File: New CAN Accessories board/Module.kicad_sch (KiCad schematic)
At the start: 13 parts, among them J1 39301040, Q1 IRLML6344TRPBF

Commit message: post design review
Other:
- moved on the sheet: TPgt1
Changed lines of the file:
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@@
+	)
+	(junction
+		(at 67.31 24.13)
+		(diameter 0)
+		(color 0 0 0 0)
 	)
 	(junction
@@
 	(wire
 		(pts
+			(xy 33.02 78.74) (xy 33.02 83.82)
+		)
+		(stroke
+			(width 0)
+			(type default)
+		)
+	)
+	(wire
+		(pts
 			(xy 40.64 63.5) (xy 43.18 63.5)
 		)
@@
 	(wire
 		(pts
+			(xy 69.85 24.13) (xy 67.31 24.13)
+		)
+		(stroke
+			(width 0)
+			(type default)
+		)
+	)
+	(wire
+		(pts
 			(xy 38.1 76.2) (xy 40.64 76.2)
+		)
+		(stroke
+			(width 0)
+			(type default)
+		)
+	)
+	(wire
+		(pts
+			(xy 15.24 78.74) (xy 33.02 78.74)
 		)
 		(stroke
@@
 	(hierarchical_label "OA"
 		(shape input)
-		(at 67.31 24.13 0)
+		(at 69.85 24.13 0)
 		(effects
 			(font
@@
 	(symbol
 		(lib_id "Connector:TestPoint")
-		(at 33.02 83.82 0)
+		(at 15.24 78.74 0)
 		(unit 1)
 		(exclude_from_sim no)
@@
 		(fields_autoplaced yes)
 		(property "Reference" "TPgt1"
-			(at 35.56 79.2479 0)
+			(at 17.78 74.1679 0)
 			(effects
 				(font
@@
 		)
 		(property "Value" "TestPoint"
-			(at 35.56 81.7879 0)
+			(at 17.78 76.7079 0)
 			(effects
 				(font
@@
 		)
 		(property "Footprint" "Connector_PinHeader_1.00mm:PinHeader_1x01_P1.00mm_Vertical"
-			(at 38.1 83.82 0)
+			(at 20.32 78.74 0)
 			(effects
 				(font
@@
 		)
 		(property "Datasheet" "~"
-			(at 38.1 83.82 0)
+			(at 20.32 78.74 0)
 			(effects
 				(font
@@
 		)
 		(property "Description" "test point"
-			(at 33.02 83.82 0)
-			(effects
-				(font
+			(at 15.24 78.74 0)
+			(effects
+				(font

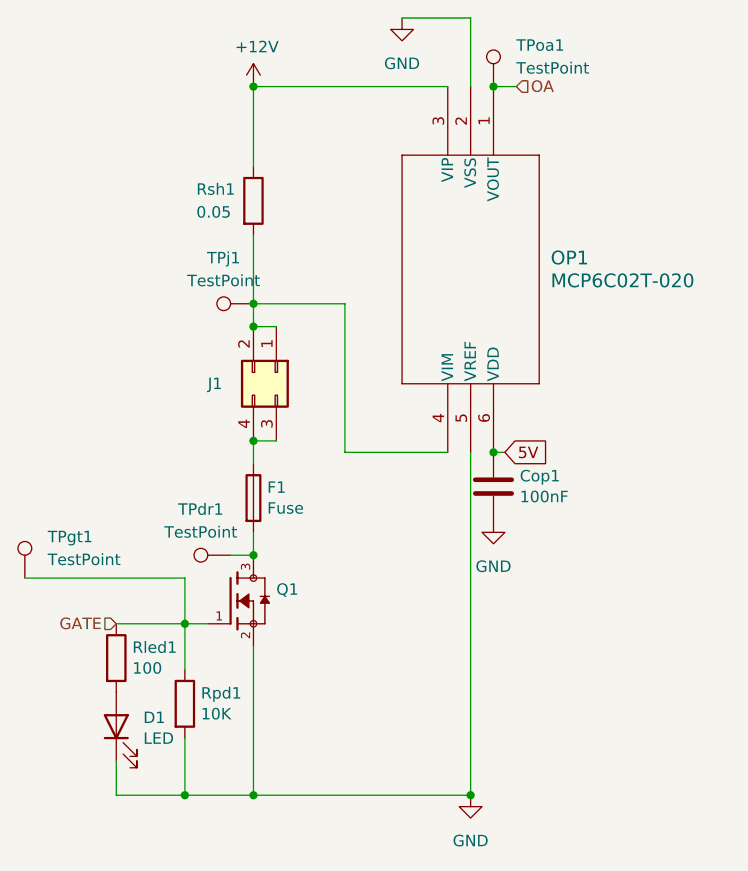
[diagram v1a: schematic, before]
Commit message: Added test points 1x12 pin and 1x8 pin
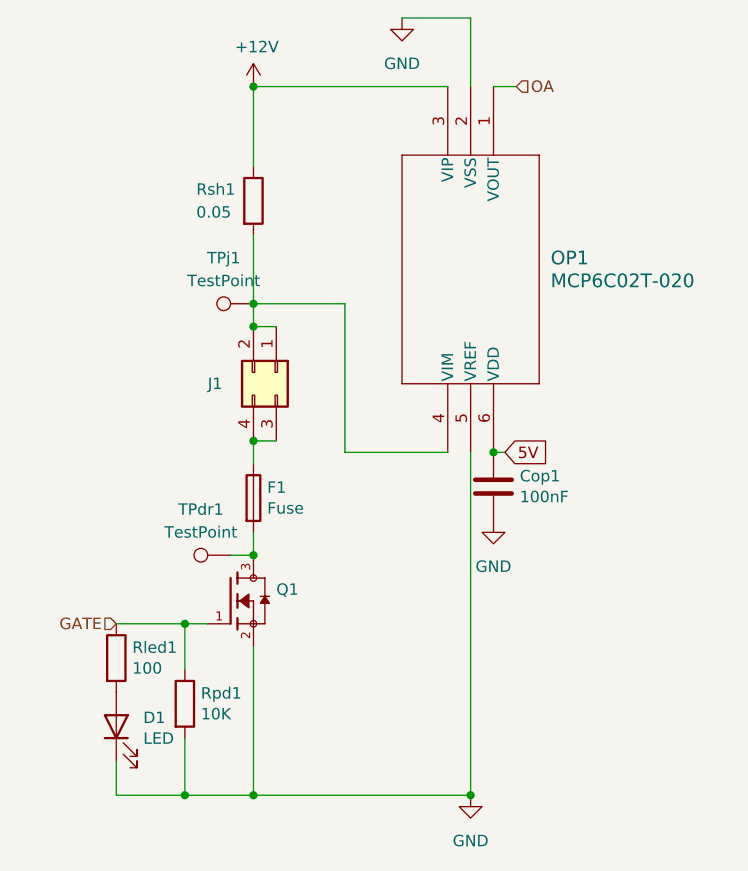
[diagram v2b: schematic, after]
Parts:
- removed TPgt1, TPoa1: TestPoint, Connector_PinHeader_1.00mm:PinHeader_1x01_P1.00mm_Vertical, symbol Connector:TestPoint
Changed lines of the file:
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@@
-	)
-	(junction
-		(at 67.31 24.13)
-		(diameter 0)
-		(color 0 0 0 0)
 	)
 	(junction
@@
 	(wire
 		(pts
-			(xy 33.02 78.74) (xy 33.02 83.82)
-		)
-		(stroke
-			(width 0)
-			(type default)
-		)
-	)
-	(wire
-		(pts
 			(xy 40.64 63.5) (xy 43.18 63.5)
 		)
@@
 		(pts
 			(xy 38.1 76.2) (xy 40.64 76.2)
-		)
-		(stroke
-			(width 0)
-			(type default)
-		)
-	)
-	(wire
-		(pts
-			(xy 15.24 78.74) (xy 33.02 78.74)
 		)
 		(stroke
@@
 	)
 	(symbol
-		(lib_id "Connector:TestPoint")
-		(at 67.31 24.13 0)
-		(unit 1)
-		(exclude_from_sim no)
-		(in_bom yes)
-		(on_board yes)
-		(dnp no)
-		(fields_autoplaced yes)
-		(property "Reference" "TPoa1"
-			(at 69.85 19.5579 0)
-			(effects
-				(font
-					(size 1.27 1.27)
-				)
-				(justify left)
-			)
-		)
-		(property "Value" "TestPoint"
-			(at 69.85 22.0979 0)
-			(effects
-				(font
-					(size 1.27 1.27)
-				)
-				(justify left)
-			)
-		)
-		(property "Footprint" "Connector_PinHeader_1.00mm:PinHeader_1x01_P1.00mm_Vertical"
-			(at 72.39 24.13 0)
-			(effects
-				(font
-					(size 1.27 1.27)
-				)
-				(hide yes)
-			)
-		)
-		(property "Datasheet" "~"
-			(at 72.39 24.13 0)
-			(effects
-				(font
-					(size 1.27 1.27)
-				)
-				(hide yes)
-			)
-		)
-		(property "Description" "test point"
-			(at 67.31 24.13 0)
-			(effects
-				(font
-					(size 1.27 1.27)
-				)
-				(hide yes)
-			)
-		)
-		(pin "1"
-		)
-		(instances
-			(project "New CAN Accessories board"
-				(path "/88340f43-3f46-45a6-9393-130e00dc3071/066a2d54-ef62-4b50-bc17-9ae15f85282f"
-					(reference "TPoa3")
-					(unit 1)
-				)
-				(path "/88340f43-3f46-45a6-9393-130e00dc3071/199d9661-d77c-40a8-9127-2f77ddd20cbc"
-					(reference "TPoa2")
-					(unit 1)
-				)
-				(path "/88340f43-3f46-45a6-9393-130e00dc3071/a4a3a29c-d4d7-4a64-89ca-c4c515902e3a"
-					(reference "TPoa8")
-					(unit 1)
-				)
-				(path "/88340f43-3f46-45a6-9393-130e00dc3071/b4fef664-0317-4528-b914-9a729a4fa0cb"
-					(reference "TPoa7")
-					(unit 1)
-				)
-				(path "/88340f43-3f46-45a6-9393-130e00dc3071/df424b4d-8c7c-4d94-be97-d7e7a5882dfa"
-					(reference "TPoa6")
-					(unit 1)
-				)
-				(path "/88340f43-3f46-45a6-9393-130e00dc3071/e28dd46e-a6b0-42fd-b358-90f6a987ac56"
-					(reference "TPoa4")
-					(unit 1)
-				)
-				(path "/88340f43-3f46-45a6-9393-130e00dc3071/f4946d2d-97a8-44f8-9d9c-ff737967b4cd"
-					(reference "TPoa5")
-					(unit 1)
-				)
-				(path "/88340f43-3f46-45a6-9393-130e00dc3071/fb19124a-c234-4595-adc5-bbb1e37c8292"
-					(reference "TPoa1")
-					(unit 1)
-				)
-			)
-		)
-	)
-	(symbol
 		(lib_id "Device:Fuse")
 		(at 40.64 69.85 0)
@@
 					(unit 1)
 				)
-			)
-		)
-	)
-	(symbol
-		(lib_id "Connector:TestPoint")
-		(at 15.24 78.74 0)
-		(unit 1)
-		(exclude_from_sim no)
-		(in_bom yes)
-		(on_board yes)
-		(dnp no)
-		(fields_autoplaced yes)
-		(property "Reference" "TPgt1"
-			(at 17.78 74.1679 0)
-			(effects
-				(font
-					(size 1.27 1.27)
-				)
-				(justify left)
-			)
-		)
-		(property "Value" "TestPoint"
-			(at 17.78 76.7079 0)
-			(effects
-				(font
-					(size 1.27 1.27)
-				)
-				(justify left)
-			)
-		)
-		(property "Footprint" "Connector_PinHeader_1.00mm:PinHeader_1x01_P1.00mm_Vertical"
-			(at 20.32 78.74 0)
-			(effects
-				(font
-					(size 1.27 1.27)
-				)
-				(hide yes)
-			)
-		)
-		(property "Datasheet" "~"
-			(at 20.32 78.74 0)
-			(effects
-				(font
-					(size 1.27 1.27)
-				)
-				(hide yes)
-			)
-		)
-		(property "Description" "test point"
-			(at 15.24 78.74 0)
-			(effects
-				(font
-					(size 1.27 1.27)
-				)
-				(hide yes)
-			)
-		)
-		(pin "1"
-		)
-		(instances
-			(project "New CAN Accessories board"
-				(path "/88340f43-3f46-45a6-9393-130e00dc3071/066a2d54-ef62-4b50-bc17-9ae15f85282f"
-					(reference "TPgt3")
-					(unit 1)
-				)
-				(path "/88340f43-3f46-45a6-9393-130e00dc3071/199d9661-d77c-40a8-9127-2f77ddd20cbc"
-					(reference "TPgt2")
-					(unit 1)
-				)
-				(path "/88340f43-3f46-45a6-9393-130e00dc3071/a4a3a29c-d4d7-4a64-89ca-c4c515902e3a"
-					(reference "TPgt8")
-					(unit 1)
-				)
-				(path "/88340f43-3f46-45a6-9393-130e00dc3071/b4fef664-0317-4528-b914-9a729a4fa0cb"
-					(reference "TPgt7")
-					(unit 1)
-				)
-				(path "/88340f43-3f46-45a6-9393-130e00dc3071/df424b4d-8c7c-4d94-be97-d7e7a5882dfa"
-					(reference "TPgt6")
-					(unit 1)
-				)
-				(path "/88340f43-3f46-45a6-9393-130e00dc3071/e28dd46e-a6b0-42fd-b358-90f6a987ac56"
-					(reference "TPgt4")
-					(unit 1)
-				)
-				(path "/88340f43-3f46-45a6-9393-130e00dc3071/f4946d2d-97a8-44f8-9d9c-ff737967b4cd"
-					(reference "TPgt5")
-					(unit 1)
-				)
-				(path "/88340f43-3f46-45a6-9393-130e00dc3071/fb19124a-c234-4595-adc5-bbb1e37c8292"
-					(reference "TPgt1")
-					(unit 1)
-				)

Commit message: Added two 1x4 pin headers for J1-J8 - also fixed CAN module
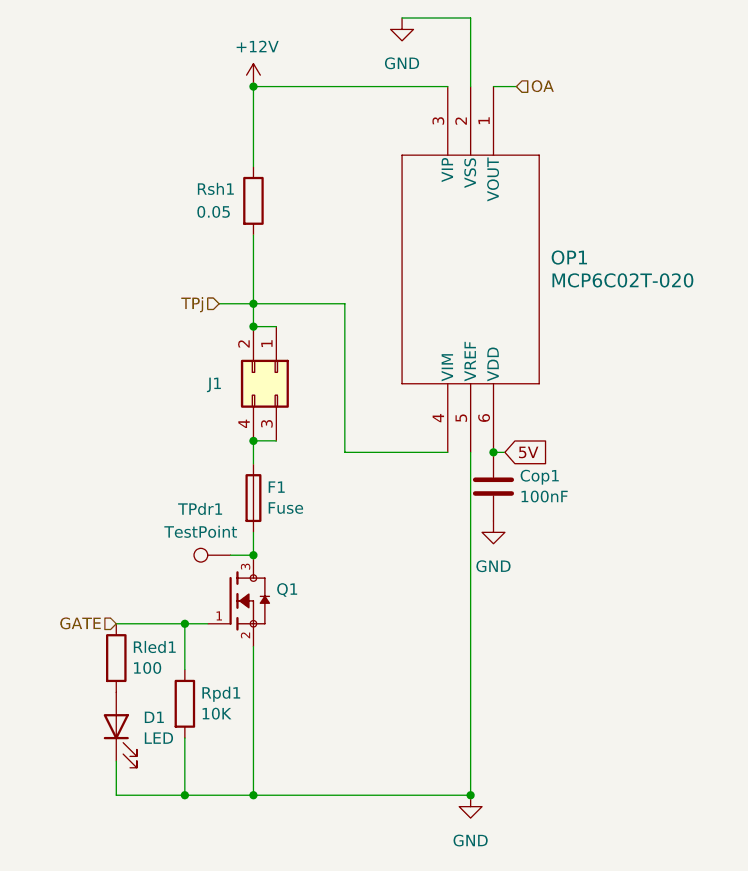
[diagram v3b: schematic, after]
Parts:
- removed TPj1: TestPoint, Connector_PinHeader_1.00mm:PinHeader_1x01_P1.00mm_Vertical, symbol Connector:TestPoint
- TPdr1: footprint Connector_PinHeader_1.00mm:PinHeader_1x01_P1.00mm_Vertical -> Connector_PinHeader_2.54mm:PinHeader_1x01_P2.54mm_Vertical
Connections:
- net TPj: now reaches J1.1 (Pin_1), J1.2 (Pin_2), OP1.4 (VIM), Rsh1.2
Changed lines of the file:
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@@
+	(wire
+		(pts
+			(xy 36.83 48.26) (xy 40.64 48.26)
+		)
+		(stroke
+			(width 0)
+			(type default)
+		)
+	)
 	(wire
 		(pts
@@
 				(hide yes)
 			)
+		)
+	)
+	(hierarchical_label "TPj"
+		(shape input)
+		(at 36.83 48.26 180)
+		(effects
+			(font
+				(size 1.27 1.27)
+			)
+			(justify right)
 		)
 	)
@@
 			)
 		)
-		(property "Footprint" "Connector_PinHeader_1.00mm:PinHeader_1x01_P1.00mm_Vertical"
+		(property "Footprint" "Connector_PinHeader_2.54mm:PinHeader_1x01_P2.54mm_Vertical"
 			(at 38.1 71.12 0)
 			(effects
@@
 				)
 				(hide yes)
+			)
+		)
+		(property "Purpose" ""
+			(at 38.1 76.2 0)
+			(effects
+				(font
+					(size 1.27 1.27)
+				)
 			)
 		)
@@
 					(unit 1)
 				)
-			)
-		)
-	)
-	(symbol
-		(lib_id "Connector:TestPoint")
-		(at 40.64 48.26 90)
-		(unit 1)
-		(exclude_from_sim no)
-		(in_bom yes)
-		(on_board yes)
-		(dnp no)
-		(fields_autoplaced yes)
-		(property "Reference" "TPj1"
-			(at 37.338 43.18 90)
-			(effects
-				(font
-					(size 1.27 1.27)
-				)
-			)
-		)
-		(property "Value" "TestPoint"
-			(at 37.338 45.72 90)
-			(effects
-				(font
-					(size 1.27 1.27)
-				)
-			)
-		)
-		(property "Footprint" "Connector_PinHeader_1.00mm:PinHeader_1x01_P1.00mm_Vertical"
-			(at 40.64 43.18 0)
-			(effects
-				(font
-					(size 1.27 1.27)
-				)
-				(hide yes)
-			)
-		)
-		(property "Datasheet" "~"
-			(at 40.64 43.18 0)
-			(effects
-				(font
-					(size 1.27 1.27)
-				)
-				(hide yes)
-			)
-		)
-		(property "Description" "test point"
-			(at 40.64 48.26 0)
-			(effects
-				(font
-					(size 1.27 1.27)
-				)
-				(hide yes)
-			)
-		)
-		(pin "1"
-		)
-		(instances
-			(project "New CAN Accessories board"
-				(path "/88340f43-3f46-45a6-9393-130e00dc3071/066a2d54-ef62-4b50-bc17-9ae15f85282f"
-					(reference "TPj3")
-					(unit 1)
-				)
-				(path "/88340f43-3f46-45a6-9393-130e00dc3071/199d9661-d77c-40a8-9127-2f77ddd20cbc"
-					(reference "TPj2")
-					(unit 1)
-				)
-				(path "/88340f43-3f46-45a6-9393-130e00dc3071/a4a3a29c-d4d7-4a64-89ca-c4c515902e3a"
-					(reference "TPj8")
-					(unit 1)
-				)
-				(path "/88340f43-3f46-45a6-9393-130e00dc3071/b4fef664-0317-4528-b914-9a729a4fa0cb"
-					(reference "TPj7")
-					(unit 1)
-				)
-				(path "/88340f43-3f46-45a6-9393-130e00dc3071/df424b4d-8c7c-4d94-be97-d7e7a5882dfa"
-					(reference "TPj6")
-					(unit 1)
-				)
-				(path "/88340f43-3f46-45a6-9393-130e00dc3071/e28dd46e-a6b0-42fd-b358-90f6a987ac56"
-					(reference "TPj4")
-					(unit 1)
-				)
-				(path "/88340f43-3f46-45a6-9393-130e00dc3071/f4946d2d-97a8-44f8-9d9c-ff737967b4cd"
-					(reference "TPj5")
-					(unit 1)
-				)
-				(path "/88340f43-3f46-45a6-9393-130e00dc3071/fb19124a-c234-4595-adc5-bbb1e37c8292"
-					(reference "TPj1")
-					(unit 1)
-				)

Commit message: added TVS diode to schematic
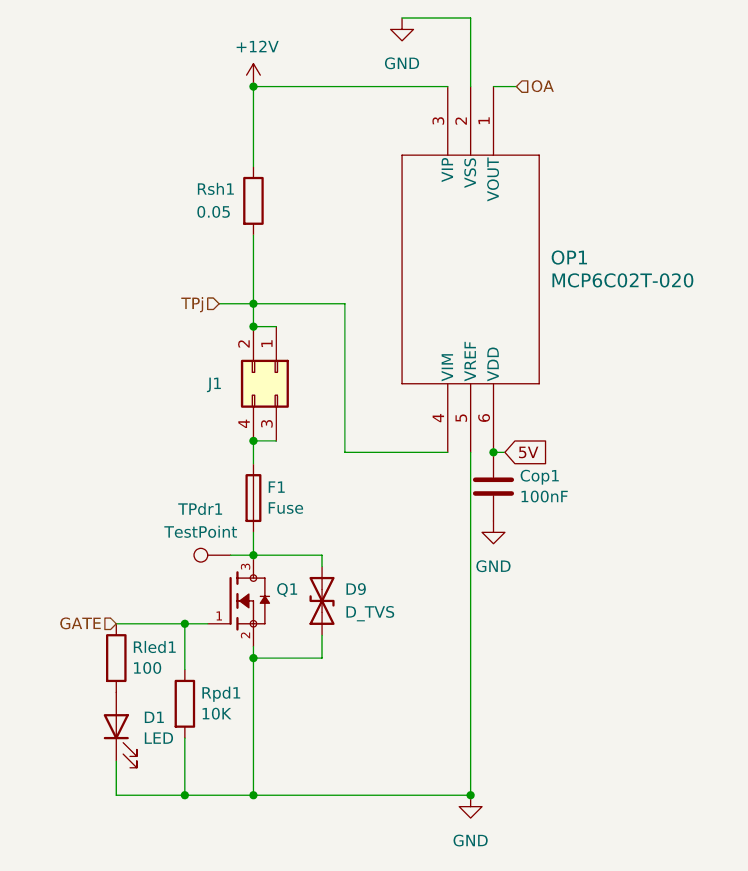
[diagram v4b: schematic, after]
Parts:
- added D9: D_TVS, symbol Device:D_TVS
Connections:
- net GND: now also D9.1 (A1)
- net at F1.2, Q1.3, TPdr1.1: now also D9.2 (A2)
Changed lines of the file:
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@@
+	)
+	(junction
+		(at 40.64 87.63)
+		(diameter 0)
+		(color 0 0 0 0)
 	)
 	(junction
@@
 	(wire
 		(pts
+			(xy 40.64 87.63) (xy 40.64 102.87)
+		)
+		(stroke
+			(width 0)
+			(type default)
+		)
+	)
+	(wire
+		(pts
 			(xy 25.4 102.87) (xy 33.02 102.87)
 		)
@@
 	(wire
 		(pts
+			(xy 48.26 87.63) (xy 40.64 87.63)
+		)
+		(stroke
+			(width 0)
+			(type default)
+		)
+	)
+	(wire
+		(pts
 			(xy 33.02 83.82) (xy 33.02 88.9)
 		)
@@
 	(wire
 		(pts
+			(xy 40.64 76.2) (xy 48.26 76.2)
+		)
+		(stroke
+			(width 0)
+			(type default)
+		)
+	)
+	(wire
+		(pts
 			(xy 50.8 64.77) (xy 50.8 48.26)
 		)
@@
 	(wire
 		(pts
+			(xy 48.26 76.2) (xy 48.26 77.47)
+		)
+		(stroke
+			(width 0)
+			(type default)
+		)
+	)
+	(wire
+		(pts
 			(xy 64.77 16.51) (xy 57.15 16.51)
 		)
@@
 	(wire
 		(pts
+			(xy 48.26 85.09) (xy 48.26 87.63)
+		)
+		(stroke
+			(width 0)
+			(type default)
+		)
+	)
+	(wire
+		(pts
 			(xy 62.23 64.77) (xy 50.8 64.77)
 		)
@@
 	(wire
 		(pts
-			(xy 40.64 86.36) (xy 40.64 102.87)
+			(xy 40.64 86.36) (xy 40.64 87.63)
 		)
 		(stroke
@@
 					(unit 1)
 				)
+			)
+		)
+	)
+	(symbol
+		(lib_id "Device:D_TVS")
+		(at 48.26 81.28 90)
+		(unit 1)
+		(exclude_from_sim no)
+		(in_bom yes)
+		(on_board yes)
+		(dnp no)
+		(fields_autoplaced yes)
+		(property "Reference" "D9"
+			(at 50.8 80.0099 90)
+			(effects
+				(font
+					(size 1.27 1.27)
+				)
+				(justify right)
+			)
+		)
+		(property "Value" "D_TVS"
+			(at 50.8 82.5499 90)
+			(effects
+				(font
+					(size 1.27 1.27)
+				)
+				(justify right)
+			)
+		)
+		(property "Footprint" ""
+			(at 48.26 81.28 0)
+			(effects
+				(font
+					(size 1.27 1.27)
+				)
+				(hide yes)
+			)
+		)
+		(property "Datasheet" "~"
+			(at 48.26 81.28 0)
+			(effects
+				(font
+					(size 1.27 1.27)
+				)
+				(hide yes)
+			)
+		)
+		(property "Description" "Bidirectional transient-voltage-suppression diode"
+			(at 48.26 81.28 0)
+			(effects
+				(font
+					(size 1.27 1.27)
+				)
+				(hide yes)
+			)
+		)
+		(pin "1"
+		)
+		(pin "2"
+		)
+		(instances
+			(project ""
+				(path "/88340f43-3f46-45a6-9393-130e00dc3071/066a2d54-ef62-4b50-bc17-9ae15f85282f"
+					(reference "D11")
+					(unit 1)
+				)
+				(path "/88340f43-3f46-45a6-9393-130e00dc3071/199d9661-d77c-40a8-9127-2f77ddd20cbc"
+					(reference "D10")
+					(unit 1)
+				)
+				(path "/88340f43-3f46-45a6-9393-130e00dc3071/a4a3a29c-d4d7-4a64-89ca-c4c515902e3a"
+					(reference "D16")
+					(unit 1)
+				)
+				(path "/88340f43-3f46-45a6-9393-130e00dc3071/b4fef664-0317-4528-b914-9a729a4fa0cb"
+					(reference "D15")
+					(unit 1)
+				)
+				(path "/88340f43-3f46-45a6-9393-130e00dc3071/df424b4d-8c7c-4d94-be97-d7e7a5882dfa"
+					(reference "D14")
+					(unit 1)
+				)
+				(path "/88340f43-3f46-45a6-9393-130e00dc3071/e28dd46e-a6b0-42fd-b358-90f6a987ac56"
+					(reference "D12")
+					(unit 1)
+				)
+				(path "/88340f43-3f46-45a6-9393-130e00dc3071/f4946d2d-97a8-44f8-9d9c-ff737967b4cd"
+					(reference "D13")
+					(unit 1)
+				)
+				(path "/88340f43-3f46-45a6-9393-130e00dc3071/fb19124a-c234-4595-adc5-bbb1e37c8292"
+					(reference "D9")
+					(unit 1)
+				)
